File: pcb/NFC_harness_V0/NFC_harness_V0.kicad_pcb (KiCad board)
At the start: 2 copper layers, 39.3 x 32 mm, 33 parts, among them J1 armed, J2 programmer, J3 Vin, J4 triggerd, J5 sender, J6 detector, J7 triggerd, Q1 MMBT3904, U1 ATtiny202-SS, U4 TPS613221ADBV

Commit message: initial commit - with tiny, will be changed to pico
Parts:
- removed C14: 4.7u, Capacitor_SMD:C_1206_3216Metric
- removed C2, C5, C9: 100n, Capacitor_SMD:C_0805_2012Metric
- removed C3: 10u, Capacitor_SMD:C_0805_2012Metric
- removed the H1 at (118.0, 110.9)
- removed the H1 at (83.7, 110.3)
- removed the H1 at (117.8, 83.5)
- removed J1: armed, Connector_PinHeader_2.54mm:PinHeader_1x02_P2.54mm_Vertical
- removed J2: programmer, Connector_PinHeader_2.54mm:PinHeader_1x03_P2.54mm_Vertical
- removed J4, J7: triggerd, Connector_PinHeader_2.54mm:PinHeader_1x02_P2.54mm_Vertical
- removed J5: sender, Connector_PinHeader_2.54mm:PinHeader_1x03_P2.54mm_Vertical
- removed J6: detector, Connector_PinHeader_2.54mm:PinHeader_1x03_P2.54mm_Vertical
- removed L1: 6.8 uH, Inductor Coilcraft:L_Coilcraft_LPS4018
- removed Q1: MMBT3904, Package_TO_SOT_SMD:SOT-23
- removed R1: 1k, Resistor_SMD:R_0805_2012Metric
- removed R11, R9: 470k, Resistor_SMD:R_0805_2012Metric
- removed R2, R3, R7: 220, Resistor_SMD:R_0805_2012Metric
- removed R4, R5: 100k, Resistor_SMD:R_0805_2012Metric
- removed R6: 1M, Resistor_SMD:R_0805_2012Metric
- removed U1: ATtiny202-SS, Package_SO:SOIC-8_3.9x4.9mm_P1.27mm
- removed U4: TPS613221ADBV, Package_TO_SOT_SMD:SOT-23-5
- added A1: RaspberryPi_Pico_W, Module_RaspberryPi_Pico:RaspberryPi_Pico_W_SMD, F.Cu at (123.5, 99.5)
- moved C4 31.6 mm to (75.0, 110.5), turned to 0 degrees
- moved R10 24.9 mm to (75.6, 107.3)
- moved R8 22.3 mm to (75.6, 104.0)
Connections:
- C4 pad 1: Vcc_5V -> /Vcc_5V
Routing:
- net Vcc_5V: track 65.2 -> 0.00 mm
- net Net-(J5-Pin_2): track 40.6 -> 0.00 mm
- net Net-(U1-PA6): track 18.5 -> 0.00 mm
- net Net-(J2-Pin_3): track 14.3 -> 0.00 mm
- net Net-(Q1-B): track 9.51 -> 0.00 mm
- net Net-(Q1-C): track 8.97 -> 0.00 mm
- net Net-(U1-PA3): track 8.66 -> 0.00 mm
- net Net-(J2-Pin_2): track 8.55 -> 0.00 mm
- net Net-(J4-Pin_2): track 8.35 -> 0.00 mm
- net Net-(U1-PA2): track 7.51 -> 0.00 mm
- net Net-(J3-Pin_2): track 9.01 -> 3.06 mm
- net Net-(U4-SW): track 4.69 -> 0.00 mm
- net Net-(J7-Pin_2): track 4.07 -> 0.00 mm
- net Net-(J1-Pin_2): track 3.96 -> 0.00 mm
- net Net-(J6-Pin_2): track 2.79 -> 0.00 mm
- removed copper zone on B.Cu, net GND
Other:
- outline, holes or cut-outs redrawn

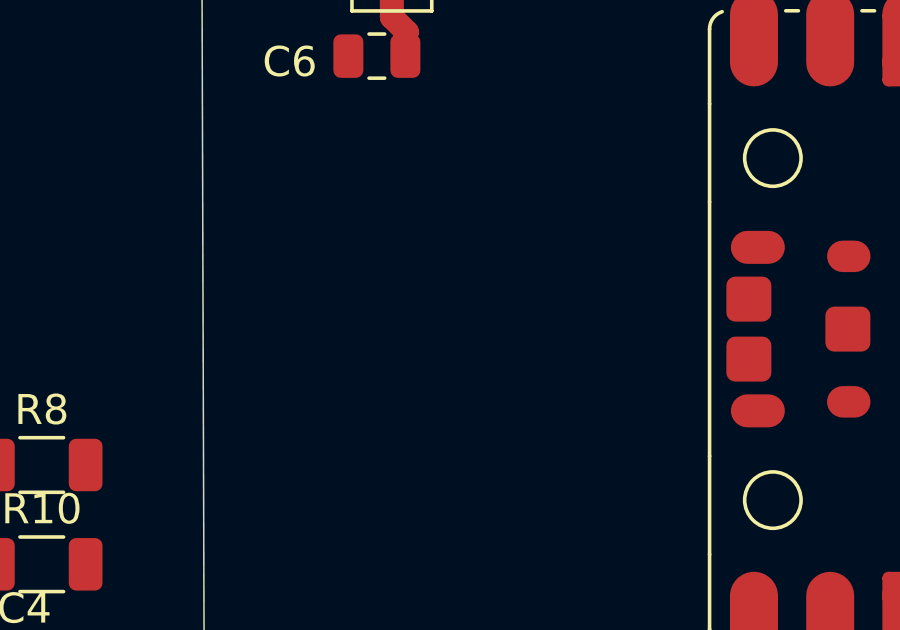
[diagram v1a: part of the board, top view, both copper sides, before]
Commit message: added i2c to main.c
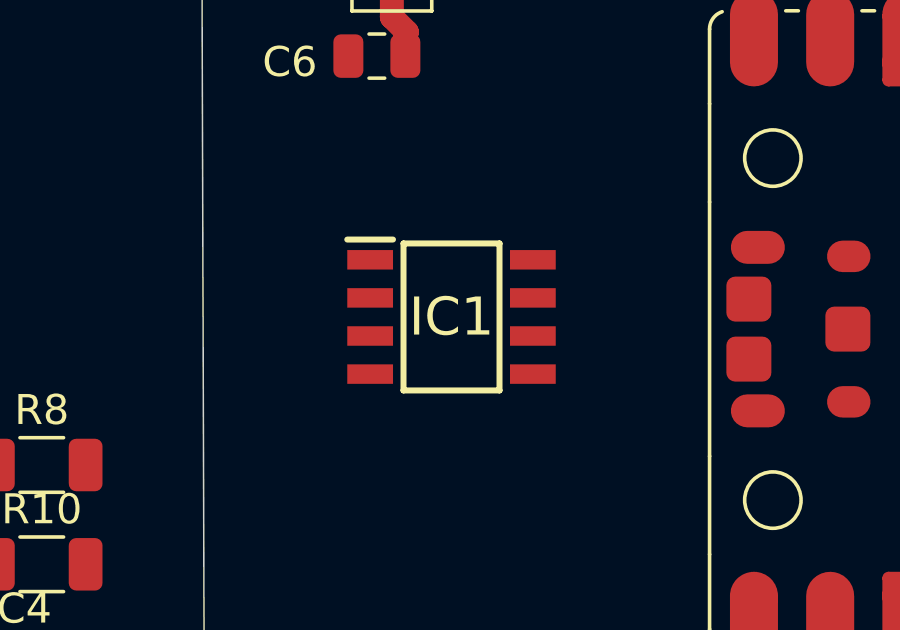
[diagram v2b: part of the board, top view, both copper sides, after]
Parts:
- added IC1: ST25DV04KC-IE6S3, ST25DV04KC-IE6S3:SOIC127P600X175-8N, F.Cu at (89.3, 99.1)

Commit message: pcb work
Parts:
- removed C4: 100n, Capacitor_SMD:C_0805_2012Metric
- removed C6: 10u, Capacitor_SMD:C_0805_2012Metric
- removed H1: MountingHole, MountingHole:MountingHole_2.1mm
- removed R10, R8: 0, Resistor_SMD:R_1206_3216Metric
- added C1: 100n, Capacitor_SMD:C_0805_2012Metric, F.Cu at (135.9, 88.0)
- added R1: 4k7, Resistor_SMD:R_1206_3216Metric, F.Cu at (125.4, 88.9)
- added R2: 4k7, Resistor_SMD:R_1206_3216Metric, F.Cu at (122.5, 84.5)
- moved J3 44.9 mm to (131.8, 79.1), turned to -90 degrees
- moved IC1 43.6 mm to (130.5, 84.8), turned to -90 degrees
- moved A1 3.92 mm to (121.4, 102.8)
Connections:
- A1 pad 13: Net-(A1-GND-Pad13) -> GND
- A1 pad 18: Net-(A1-GND-Pad13) -> GND
- A1 pad 23: Net-(A1-GND-Pad13) -> GND
- A1 pad 24: unconnected-(A1-GPIO18-Pad24) -> Net-(A1-GPIO18)
- A1 pad 25: unconnected-(A1-GPIO19-Pad25) -> Net-(A1-GPIO19)
- A1 pad 26: unconnected-(A1-GPIO20-Pad26) -> Net-(A1-GPIO20)
- A1 pad 27: unconnected-(A1-GPIO21-Pad27) -> Net-(A1-GPIO21)
- A1 pad 28: Net-(A1-GND-Pad13) -> GND
- A1 pad 3: Net-(A1-GND-Pad13) -> GND
- A1 pad 33: unconnected-(A1-AGND-Pad33) -> GND
- A1 pad 36: unconnected-(A1-3V3-Pad36) -> Net-(A1-3V3)
- A1 pad 38: Net-(A1-GND-Pad13) -> GND
- A1 pad 8: Net-(A1-GND-Pad13) -> GND
- A1 pad D2: Net-(A1-GND-Pad13) -> GND
- IC1 pad 2: unconnected-(IC1-AC0-Pad2) -> Net-(IC1-AC0)
- IC1 pad 3: unconnected-(IC1-AC1-Pad3) -> Net-(IC1-AC1)
- IC1 pad 4: unconnected-(IC1-VSS-Pad4) -> GND
- IC1 pad 5: unconnected-(IC1-SDA-Pad5) -> Net-(A1-GPIO20)
- IC1 pad 6: unconnected-(IC1-SCL-Pad6) -> Net-(A1-GPIO21)
- IC1 pad 7: unconnected-(IC1-GPO_(OPEN_DRAIN)-Pad7) -> Net-(A1-GPIO19)
- IC1 pad 8: unconnected-(IC1-VCC-Pad8) -> Net-(A1-GPIO18)
- J3 pad 1: GND -> Net-(IC1-AC0)
- J3 pad 2: Net-(J3-Pin_2) -> Net-(IC1-AC1)
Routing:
- net Net-(A1-3V3): track 0.00 -> 24.8 mm
- net Net-(A1-GPIO21): track 0.00 -> 21.6 mm
- net Net-(A1-GPIO18): track 0.00 -> 11.3 mm
- net Net-(A1-GPIO20): track 0.00 -> 10.5 mm
- net Net-(A1-GPIO19): track 0.00 -> 8.81 mm
- net Net-(IC1-AC1): track 0.00 -> 3.30 mm
- net Net-(IC1-AC0): track 0.00 -> 3.27 mm
- net Net-(J3-Pin_2): track 3.06 -> 0.00 mm
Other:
- board size 39.3 x 32 mm -> 52.7 x 38.1 mm

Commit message: cam job output
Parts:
- added C13: 4.7u, Capacitor_SMD:C_1206_3216Metric, F.Cu at (140.9, 86.9)
- added C2: 10p, Capacitor_SMD:C_0805_2012Metric, F.Cu at (121.8, 80.3)
- added C3: JZ400, JZ400:JZ400, F.Cu at (125.7, 80.0)
- added C4: 4.7u, Capacitor_SMD:C_1206_3216Metric, F.Cu at (135.9, 83.4)
- added J1: energy harvest, Connector_PinHeader_2.54mm:PinHeader_1x02_P2.54mm_Vertical, F.Cu at (141.9, 81.8)
- added R3: 0, Resistor_SMD:R_1206_3216Metric, F.Cu at (118.5, 88.7)
- J3: value Vin -> antenna
- moved J3 13.1 mm to (118.7, 78.9), turned to 0 degrees
- moved R2 0.46 mm to (122.6, 85.0)
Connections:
- IC1 pad 1: unconnected-(IC1-V_EH-Pad1) -> Net-(IC1-V_EH)
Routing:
- net Net-(IC1-V_EH): track 0.00 -> 19.4 mm
- net Net-(IC1-AC0): track 3.27 -> 16.8 mm
- net Net-(IC1-AC1): track 3.30 -> 15.2 mm
- net Net-(A1-GPIO18): track 11.3 -> 13.7 mm
- net Net-(A1-3V3): track 24.8 -> 25.6 mm

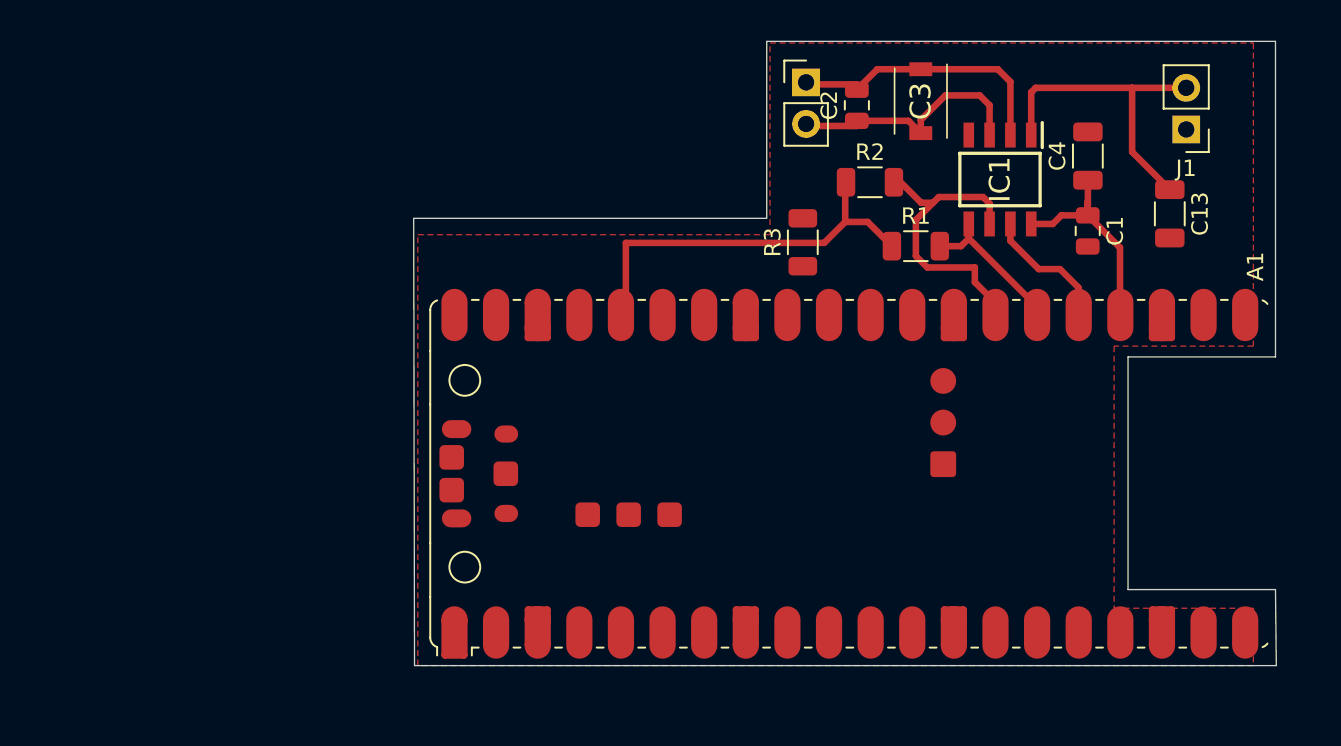
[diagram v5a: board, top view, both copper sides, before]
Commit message: pcb: update NFC harness and add Taster 9313 footprint
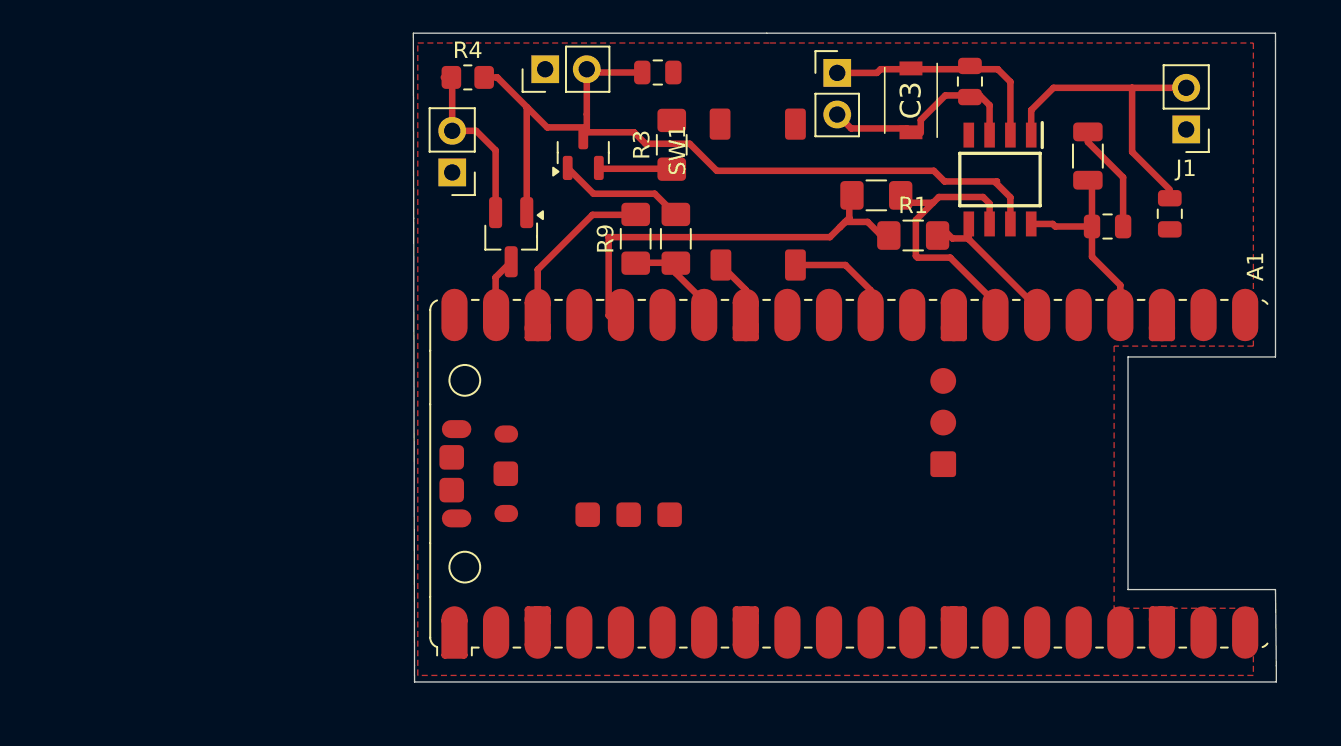
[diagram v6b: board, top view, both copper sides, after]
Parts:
- added C5: 22n, Capacitor_SMD:C_0805_2012Metric, F.Cu at (109.7, 78.3)
- added J2: battery, Connector_PinHeader_2.54mm:PinHeader_1x02_P2.54mm_Vertical, F.Cu at (97.1, 84.4)
- added J4: always on, Connector_PinHeader_2.54mm:PinHeader_1x02_P2.54mm_Vertical, F.Cu at (102.8, 78.1)
- added Q1: TSM260P02CX, Package_TO_SOT_SMD:SOT-23_Handsoldering, F.Cu at (100.7, 88.3)
- added Q2: MMBT3904, Package_TO_SOT_SMD:SOT-23, F.Cu at (105.1, 83.2)
- added R4: 1M, Resistor_SMD:R_0805_2012Metric_Pad1.20x1.40mm_HandSolder, F.Cu at (98.0, 78.6)
- added R5: 100k, Fuse:Fuse_1206_3216Metric_Pad1.42x1.75mm_HandSolder, F.Cu at (110.8, 88.5)
- added R9: 50k, Fuse:Fuse_1206_3216Metric_Pad1.42x1.75mm_HandSolder, F.Cu at (108.3, 88.5)
- added SW1: SW_Push, Taster:Taster 9313, F.Cu at (115.8, 85.8)
- C13: value 4.7u -> 100n; footprint Capacitor_SMD:C_1206_3216Metric -> Capacitor_SMD:C_0805_2012Metric
- R1, R2, R3: footprint Resistor_SMD:R_1206_3216Metric -> Fuse:Fuse_1206_3216Metric_Pad1.42x1.75mm_HandSolder
- moved R3 9.97 mm to (110.5, 82.7)
- moved C2 7.05 mm to (128.7, 78.8)
- moved J3 1.99 mm to (120.6, 78.3)
- moved C1 1.24 mm to (137.1, 87.7), turned to 0 degrees
- moved R2 0.89 mm to (123.0, 85.8)
- moved R1 0.67 mm to (125.2, 88.2)
- moved C3 0.60 mm to (125.1, 80.0)
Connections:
- A1 pad 25: Net-(A1-GPIO19) -> unconnected-(A1-GPIO19-Pad25)
- A1 pad 30: unconnected-(A1-RUN-Pad30) -> Net-(A1-RUN)
- A1 pad 34: unconnected-(A1-GPIO28_ADC2-Pad34) -> Net-(A1-GPIO28_ADC2)
- A1 pad 39: unconnected-(A1-VSYS-Pad39) -> Net-(A1-VSYS)
- IC1 pad 7: Net-(A1-GPIO19) -> Net-(IC1-GPO_(OPEN_DRAIN))
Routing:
- net Net-(IC1-GPO_(OPEN_DRAIN)): track 0.00 -> 50.1 mm
- net GND: track 0.00 -> 26.8 mm
- net Vbatt: track 0.00 -> 10.4 mm
- net Net-(A1-GPIO19): track 8.81 -> 0.00 mm
- net Net-(Q2-B): track 0.00 -> 7.79 mm
- net Net-(A1-RUN): track 0.00 -> 7.54 mm
- net Net-(A1-GPIO28_ADC2): track 0.00 -> 7.15 mm
- net Net-(A1-VSYS): track 0.00 -> 4.46 mm
- net Net-(A1-GPIO21): track 21.6 -> 17.4 mm
- net Net-(IC1-AC1): track 15.2 -> 12.6 mm
- net Net-(IC1-AC0): track 16.8 -> 14.2 mm
- net Net-(A1-GPIO20): track 10.0 -> 10.8 mm
- net Net-(A1-3V3): track 25.6 -> 26.3 mm
- net Net-(IC1-V_EH): track 19.4 -> 18.7 mm
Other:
- board size 52.7 x 38.1 mm -> 52.7 x 39.6 mm

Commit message: pcb edits
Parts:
- added R6: 0, Fuse:Fuse_1206_3216Metric_Pad1.42x1.75mm_HandSolder, F.Cu at (99.7, 89.2)
- moved Q1 3.53 mm to (101.2, 84.8)
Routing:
- net Net-(IC1-GPO_(OPEN_DRAIN)): track 50.1 -> 46.0 mm
- net Vbatt: track 10.4 -> 6.46 mm
- net Net-(A1-VSYS): track 4.46 -> 8.14 mm
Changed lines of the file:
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@@
 	(footprint "Fuse:Fuse_1206_3216Metric_Pad1.42x1.75mm_HandSolder"
 		(layer "F.Cu")
+		(at 99.7125 89.2)
+		(descr "Fuse SMD 1206 (3216 Metric), square (rectangular) end terminal, IPC-7351 nominal with elongated pad for handsoldering. (Body size source: http://www.tortai-tech.com/upload/download/2011102023233369053.pdf), generated with kicad-footprint-generator")
+		(tags "fuse handsolder")
+		(property "Reference" "R6"
+			(at 0 -1.83 0)
+			(layer "F.SilkS")
+			(hide yes)
+			(effects
+				(font
+					(size 1 1)
+					(thickness 0.15)
+				)
+			)
+		)
+		(property "Value" "0"
+			(at 0 1.83 0)
+			(layer "F.Fab")
+			(effects
+				(font
+					(size 1 1)
+					(thickness 0.15)
+				)
+			)
+		)
+		(property "Datasheet" "~"
+			(at 0 0 0)
+			(layer "F.Fab")
+			(hide yes)
+			(effects
+				(font
+					(size 1.27 1.27)
+					(thickness 0.15)
+				)
+			)
+		)
+		(property "Description" "Resistor"
+			(at 0 0 0)
+			(layer "F.Fab")
+			(hide yes)
+			(effects
+				(font
+					(size 1.27 1.27)
+					(thickness 0.15)
+				)
+			)
+		)
+		(property ki_fp_filters "R_*")
+		(sheetname "/")
+		(sheetfile "NFC_harness_V0.kicad_sch")
+		(attr smd)
+		(fp_line
+			(start -0.602064 -0.91)
+			(end 0.602064 -0.91)
+			(stroke
+				(width 0.12)
+				(type solid)
+			)
+			(layer "F.SilkS")
+		)
+		(fp_line
+			(start -0.602064 0.91)
+			(end 0.602064 0.91)
+			(stroke
+				(width 0.12)
+				(type solid)
+			)
+			(layer "F.SilkS")
+		)
+		(fp_line
+			(start -2.45 -1.13)
+			(end 2.45 -1.13)
+			(stroke
+				(width 0.05)
+				(type solid)
+			)
+			(layer "F.CrtYd")
+		)
+		(fp_line
+			(start -2.45 1.13)
+			(end -2.45 -1.13)
+			(stroke
+				(width 0.05)
+				(type solid)
+			)
+			(layer "F.CrtYd")
+		)
+		(fp_line
+			(start 2.45 -1.13)
+			(end 2.45 1.13)
+			(stroke
+				(width 0.05)
+				(type solid)
+			)
+			(layer "F.CrtYd")
+		)
+		(fp_line
+			(start 2.45 1.13)
+			(end -2.45 1.13)
+			(stroke
+				(width 0.05)
+				(type solid)
+			)
+			(layer "F.CrtYd")
+		)
+		(fp_line
+			(start -1.6 -0.8)
+			(end 1.6 -0.8)
+			(stroke
+				(width 0.1)
+				(type solid)
+			)
+			(layer "F.Fab")
+		)
+		(fp_line
+			(start -1.6 0.8)
+			(end -1.6 -0.8)
+			(stroke
+				(width 0.1)
+				(type solid)
+			)
+			(layer "F.Fab")
+		)
+		(fp_line
+			(start 1.6 -0.8)
+			(end 1.6 0.8)
+			(stroke
+				(width 0.1)
+				(type solid)
+			)
+			(layer "F.Fab")
+		)
+		(fp_line
+			(start 1.6 0.8)
+			(end -1.6 0.8)
+			(stroke
+				(width 0.1)
+				(type solid)
+			)
+			(layer "F.Fab")
+		)
+		(fp_text user "${REFERENCE}"
+			(at 0 0 0)
+			(layer "F.Fab")
+			(effects
+				(font
+					(size 0.8 0.8)
+					(thickness 0.12)
+				)
+			)
+		)
+		(pad "1" smd roundrect
+			(at -1.4875 0)
+			(size 1.425 1.75)
+			(layers "F.Cu" "F.Mask" "F.Paste")
+			(roundrect_rratio 0.175439)
+			(net 1 "GND")
+			(pintype "passive")
+		)
+		(pad "2" smd roundrect
+			(at 1.4875 0)
+			(size 1.425 1.75)
+			(layers "F.Cu" "F.Mask" "F.Paste")
+			(roundrect_rratio 0.175439)
+			(net 1 "GND")
+			(pintype "passive")
+		)
+		(embedded_fonts no)
+		(model "${KICAD9_3DMODEL_DIR}/Fuse.3dshapes/Fuse_1206_3216Metric.step"
+			(offset
+				(xyz 0 0 0)
+			)
+			(scale
+				(xyz 1 1 1)
+			)
+			(rotate
+				(xyz 0 0 0)
+			)
+		)
+	)
+	(footprint "Fuse:Fuse_1206_3216Metric_Pad1.42x1.75mm_HandSolder"
+		(layer "F.Cu")
 		(at 110.75 88.45 -90)
 		(descr "Fuse SMD 1206 (3216 Metric), square (rectangular) end terminal, IPC-7351 nominal with elongated pad for handsoldering. (Body size source: http://www.tortai-tech.com/upload/download/2011102023233369053.pdf), generated with kicad-footprint-generator")
@@
 		)
 		(property "Value" "100k"
-			(at -0.35 4.65 270)
+			(at 0.1 4.95 270)
 			(layer "F.Fab")
 			(effects
@@
 			(at 0 -1.83 0)
 			(layer "F.SilkS")
+			(hide yes)
 			(effects
 				(font
@@
 			(at 0 -1.83 90)
 			(layer "F.SilkS")
+			(hide yes)
 			(effects
 				(font
@@
 			(at 0 -1.83 90)
 			(layer "F.SilkS")
+			(hide yes)
 			(effects
 				(font
@@
 			(at 0 -1.65 0)
 			(layer "F.SilkS")
+			(hide yes)
 			(effects
 				(font
@@
 		(at 115.75 85.75 90)
 		(property "Reference" "SW1"
-			(at 2.7 -4.9 90)
+			(at -0.5 -2.5 90)
 			(unlocked yes)
 			(layer "F.SilkS")
@@
 	(footprint "Package_TO_SOT_SMD:SOT-23_Handsoldering"
 		(layer "F.Cu")
-		(at 100.7 88.35 -90)
+		(at 101.15 84.85 -90)
 		(descr "SOT-23, Handsoldering")
 		(tags "SOT-23")
@@
 	)
 	(segment
-		(start 99.75 83.05)
-		(end 98.56 81.86)
-		(width 0.4)
-		(layer "F.Cu")
-		(net 36)
-	)
-	(segment
-		(start 97.1 79.1125)
-		(end 96.5875 78.6)
-		(width 0.4)
-		(layer "F.Cu")
-		(net 36)
-	)
-	(segment
-		(start 98.56 81.86)
-		(end 97.1 81.86)
+		(start 97.1 81.86)
+		(end 98.71 81.86)
 		(width 0.4)
 		(layer "F.Cu")
@@
 	)
 	(segment
-		(start 99.75 86.85)
-		(end 99.75 83.05)
+		(start 98.71 81.86)
+		(end 100.2 83.35)
 		(width 0.4)
 		(layer "F.Cu")
@@
 	)
 	(segment
-		(start 99.75 90.8)
+		(start 99.78 93.9)
 		(end 99.75 93.87)
 		(width 0.4)
@@
 	)
 	(segment
-		(start 100.7 89.85)
-		(end 99.75 90.8)
+		(start 99.75 93.87)
+		(end 99.75 87.75)
 		(width 0.4)
 		(layer "F.Cu")
@@
 	)
 	(segment
-		(start 99.75 93.87)
-		(end 99.78 93.9)
+		(start 99.75 87.75)
+		(end 101.15 86.35)
 		(width 0.4)
 		(layer "F.Cu")
@@
 	)
 	(segment
+		(start 102.1 83.35)
+		(end 102.1 81.8)
+		(width 0.4)
+		(layer "F.Cu")
+		(net 38)
+	)
+	(segment
 		(start 113.25 84.3)
 		(end 111.6 82.65)
@@
 	)
 	(segment
+		(start 102.9 81.65)
+		(end 102.575 81.325)
+		(width 0.4)
+		(layer "F.Cu")
+		(net 38)
+	)
+	(segment
 		(start 101.675 80.425)
 		(end 99.85 78.6)
@@
 	)
 	(segment
-		(start 101.65 86.85)
-		(end 101.65 80.45)
-		(width 0.4)
-		(layer "F.Cu")
-		(net 38)
-	)
-	(segment
-		(start 102.9 81.65)
+		(start 102.575 81.325)
 		(end 101.675 80.425)
 		(width 0.4)
@@
 		(width 0.4)
 		(layer "F.Cu")
+		(net 38)
+	)
+	(segment
+		(start 102.1 81.8)
+		(end 102.575 81.325)
+		(width 0.4)
+		(layer "F.Cu")
